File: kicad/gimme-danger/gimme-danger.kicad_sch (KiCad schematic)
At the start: 54 parts, among them J2 Barrel_Jack, J3 Screw_Terminal_01x06, Q1 AO3400A, Q2 AO3400A, U1 ESP32-S3-WROOM-1, U2 TPD6S300RUKR, U3 U261-241N-4BS2SS, U4 AO4407A, U5 SKRKAEE020, U6 DDTC143EUA, U7 SKRKAEE020, U8 TPS54302

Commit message: Initial partial routing
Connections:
- net VOUT: now also C10.1, U4.5 (D), U4.6 (D), U4.7 (D), U4.8 (D)
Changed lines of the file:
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@@
+    (stroke (width 0) (type default))
+  )
+  (wire (pts (xy 249.682 30.988) (xy 249.682 33.528))
     (stroke (width 0) (type default))
   )
@@
     (stroke (width 0) (type default))
   )
-  (wire (pts (xy 249.682 30.988) (xy 249.682 28.448))
+  (wire (pts (xy 249.682 28.448) (xy 249.682 30.988))
     (stroke (width 0) (type default))
   )
@@
     (stroke (width 0) (type default))
   )
-  (wire (pts (xy 249.682 33.528) (xy 249.682 30.988))
-    (stroke (width 0) (type default))
-  )
   (wire (pts (xy 140.335 64.77) (xy 140.335 69.85))
     (stroke (width 0) (type default))
@@
     (stroke (width 0) (type default))
   )
-  (wire (pts (xy 249.936 30.988) (xy 252.476 30.988))
-    (stroke (width 0) (type default))
-  )
   (wire (pts (xy 234.442 33.528) (xy 234.442 30.988))
     (stroke (width 0) (type default))
@@
     (stroke (width 0) (type default))
   )
+  (wire (pts (xy 249.682 30.988) (xy 252.476 30.988))
+    (stroke (width 0) (type default))
+  )

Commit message: Initial routing
Many issues :|
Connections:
- net CH1: now also R9.1; no longer R9.2
- net GND: now also J3.6 (Pin_6); no longer J3.2 (Pin_2)
- net OUT2: now also J3.2 (Pin_2); no longer J3.6 (Pin_6)
- net at U1.10 (GPIO17/U1TXD/ADC2_CH6): no longer R9.1
- net at U1.11 (GPIO18/U1RXD/ADC2_CH7/CLK_OUT3): no longer R10.1
- net at U1.24 (GPIO47/SPICLK_P/SUBSPICLK_P_DIFF): now also R10.1
- net at U1.25 (GPIO48/SPICLK_N/SUBSPICLK_N_DIFF): now also R9.2
- no-connect marks 41 -> 42
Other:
- moved on the sheet: C5, C6, C7, J3, R10, R11, R2, R3, R4, R9, U1, U5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

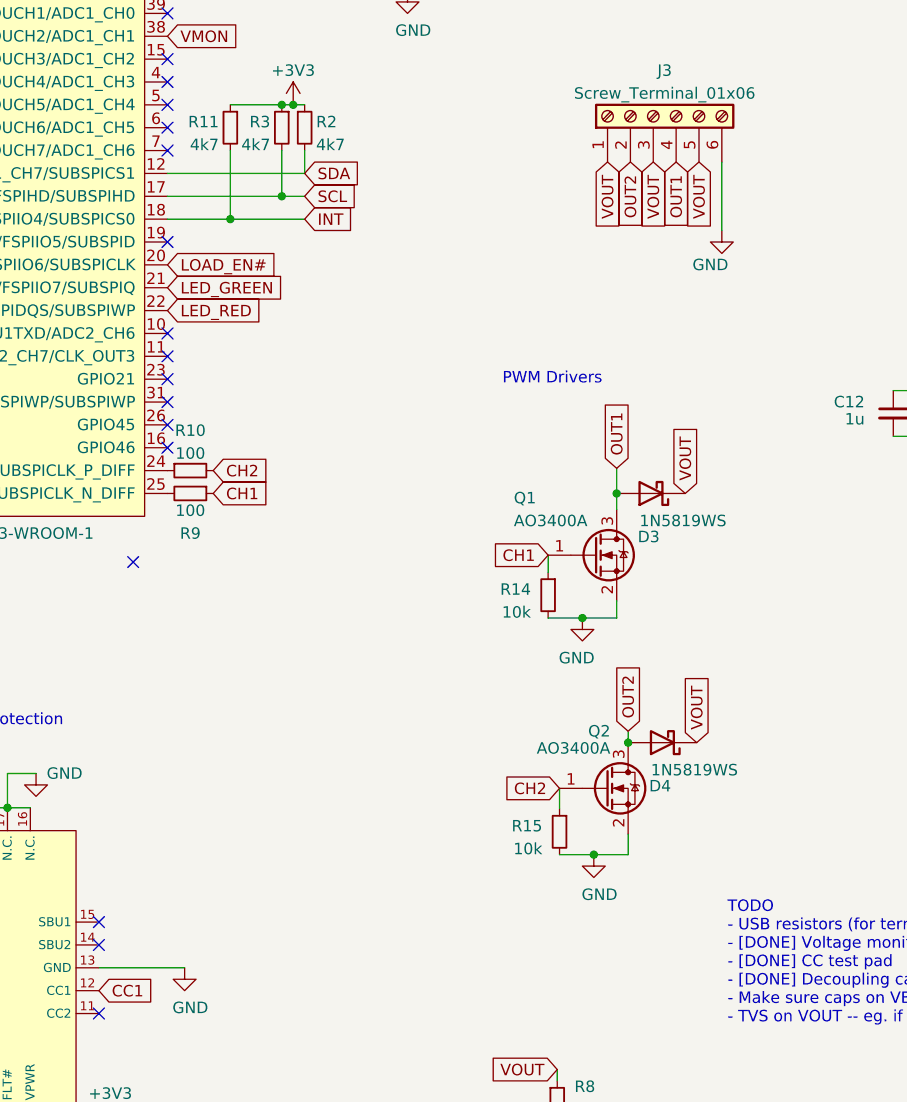
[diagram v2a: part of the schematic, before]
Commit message: Routed new output: 4 channels
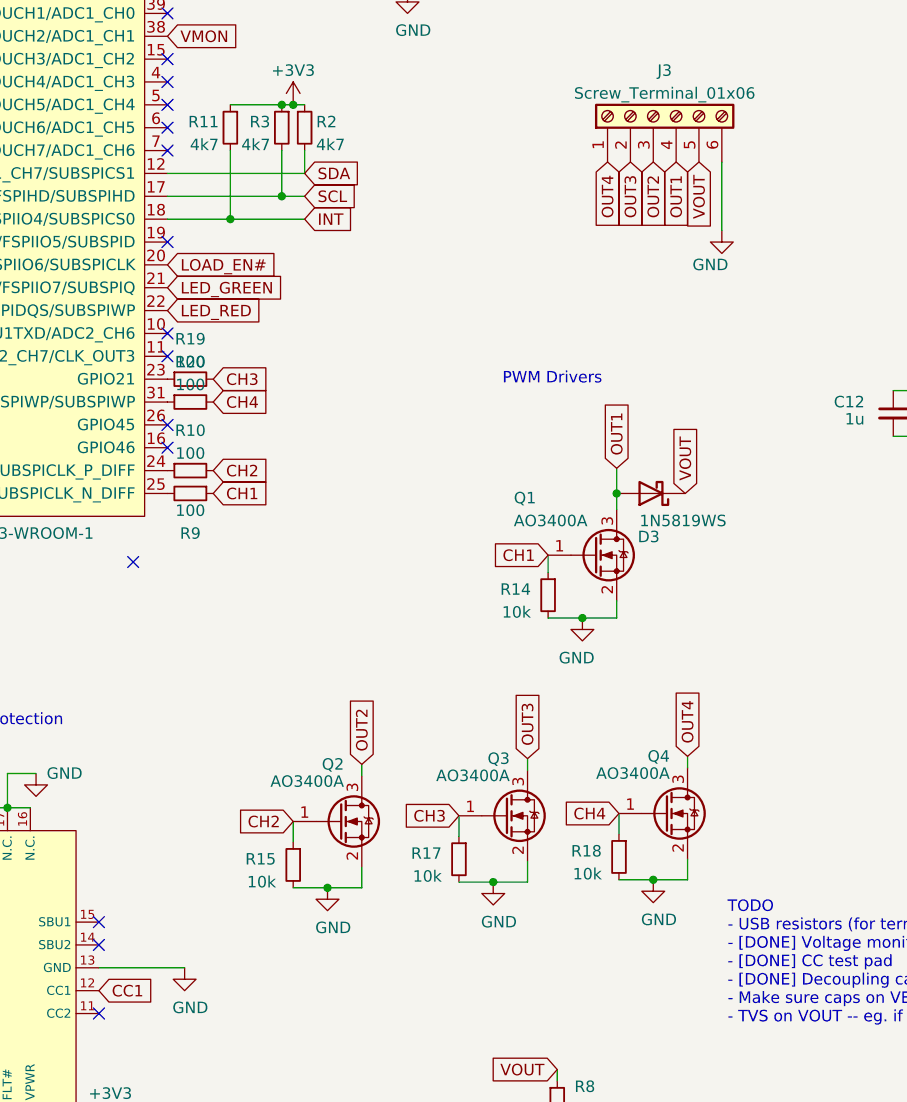
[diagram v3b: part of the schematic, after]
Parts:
- removed D4: 1N5819WS, Diode_SMD:D_SOD-323, symbol Diode:1N5819WS
- added Q3, Q4: AO3400A, Package_TO_SOT_SMD:SOT-23, symbol Transistor_FET:AO3400A
- added R17, R18: 10k, Resistor_SMD:R_0402_1005Metric, symbol Device:R_Small
- added R19, R20: 100, Resistor_SMD:R_0402_1005Metric, symbol Device:R_Small
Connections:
- net GND: now also Q3.2 (S), Q4.2 (S), R17.2, R18.2
- net OUT2: now also J3.3 (Pin_3); no longer J3.2 (Pin_2)
- net VOUT: no longer J3.1 (Pin_1), J3.3 (Pin_3)
- net at U1.23 (GPIO21): now also R19.1
- net at U1.31 (GPIO38/FSPIWP/SUBSPIWP): now also R20.1
- new net CH3: Q3.1 (G), R17.1, R19.2
- new net CH4: Q4.1 (G), R18.1, R20.2
- new net OUT3: J3.2 (Pin_2), Q3.3 (D)
- new net OUT4: J3.1 (Pin_1), Q4.3 (D)
- no-connect marks 42 -> 40
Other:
- moved on the sheet: Q2, R15

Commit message: No mo 0.2 vias -> 0.3 vias
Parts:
- C1: value 100n -> 0.1u
- D2: LCSC C2286 -> C72038
- J2: now left out of the parts list
- J3: now not fitted
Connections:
- net C_SBU2: no longer names the net of U2.2 (C_SBU2)
- net C_SBU2: no longer U3.B8 (SBU2)
- no-connect marks 40 -> 42
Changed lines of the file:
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@@
   (no_connect (at 125.095 99.06))
   (no_connect (at 252.095 86.36))
+  (no_connect (at 92.075 154.305))
   (no_connect (at 58.42 147.32))
   (no_connect (at 227.33 133.35))
@@
   (no_connect (at 125.095 58.42))
   (no_connect (at 33.655 48.26))
+  (no_connect (at 58.42 154.94))
   (no_connect (at 35.56 170.18))
   (no_connect (at 117.475 151.765))
@@
     )
   )
-  (global_label "C_SBU2" (shape input) (at 58.42 154.94 0) (fields_autoplaced)
-    (effects (font (size 1.27 1.27)) (justify left))
-    (property "Intersheetrefs" "${INTERSHEET_REFS}" (at 68.5829 154.94 0)
-      (effects (font (size 1.27 1.27)) (justify left) hide)
-    )
-  )
   (global_label "C_CC1" (shape input) (at 92.075 159.385 180) (fields_autoplaced)
     (effects (font (size 1.27 1.27)) (justify right))
@@
     )
   )
-  (global_label "C_SBU2" (shape input) (at 92.075 154.305 180) (fields_autoplaced)
-    (effects (font (size 1.27 1.27)) (justify right))
-    (property "Intersheetrefs" "${INTERSHEET_REFS}" (at 81.9121 154.305 0)
-      (effects (font (size 1.27 1.27)) (justify right) hide)
-    )
-  )
   (global_label "C_SBU1" (shape input) (at 35.56 162.56 180) (fields_autoplaced)
     (effects (font (size 1.27 1.27)) (justify right))
@@
   )
   (symbol (lib_id "Connector:Barrel_Jack") (at 143.764 187.198 0) (unit 1)
-    (in_bom yes) (on_board no) (dnp yes) (fields_autoplaced)
+    (in_bom no) (on_board no) (dnp yes) (fields_autoplaced)
     (property "Reference" "J2" (at 143.764 180.086 0)
       (effects (font (size 1.27 1.27)))
@@
       (effects (font (size 1.27 1.27)) (justify left))
     )
-    (property "Value" "100n" (at 83.82 166.3763 0)
+    (property "Value" "0.1u" (at 83.82 166.3763 0)
       (effects (font (size 1.27 1.27)) (justify left))
     )
@@
       (effects (font (size 1.27 1.27)) hide)
     )
-    (property "LCSC" "C2286" (at 185.928 38.608 90)
+    (property "LCSC" "C72038" (at 185.928 38.608 90)
       (effects (font (size 1.27 1.27)) hide)
     )
@@
   )
   (symbol (lib_id "Connector:Screw_Terminal_01x06") (at 179.07 62.23 90) (unit 1)
-    (in_bom no) (on_board yes) (dnp no)
+    (in_bom no) (on_board yes) (dnp yes)
     (property "Reference" "J3" (at 180.34 57.15 90)
       (effects (font (size 1.27 1.27)))

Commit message: Fixes DRC errors
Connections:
- no-connect marks 42 -> 43
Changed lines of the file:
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@@
   (no_connect (at 33.655 99.06))
   (no_connect (at 33.655 40.64))
+  (no_connect (at 4.445 33.655))
   (no_connect (at 35.56 147.32))
   (no_connect (at 121.285 111.76))

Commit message: Blinky kinda works! But boards needs revision...
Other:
- note added: "Errors with v0.0.1: - C14 connected after L2. It would be before - L2 too big? 47nH in luz, 470nH here. Problem or better? - Does not seem to matter - Missing Rdown on CC1?? - But FUSB doesnt seem to require it? It's the default port setting? - C6 should be 22u not 22n"
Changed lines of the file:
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@@
+    (effects (font (size 1.27 1.27)) (justify left bottom))
+  )
+  (text "Errors with v0.0.1:\n- C14 connected after L2. It would be before\n- L2 too big? 47nH in luz, 470nH here. Problem or better?\n  - Does not seem to matter\n- Missing Rdown on CC1??\n  - But FUSB doesnt seem to require it? It's the default port setting?\n- C6 should be 22u not 22n"
+    (at 307.34 107.95 0)
     (effects (font (size 1.27 1.27)) (justify left bottom))
   )
